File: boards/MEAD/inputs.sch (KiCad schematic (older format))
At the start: 13 parts, among them J3 LSHM-120-02.5-L-DV-A-N-K-TR, U10 RCLAMP0542T, U11 RCLAMP0542T, U12 RCLAMP0542T, U13 RCLAMP0542T

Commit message: Updated MEAD LA pod design with display and different protection diodes
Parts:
- removed U10, U11, U12, U13: RCLAMP0542T, symbol special-azonenberg:RCLAMP0542T
- added D10, D11, D12, D9: SP4010, symbol special-azonenberg:SP4010
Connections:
- net labels added: 5V0
- wire segments 66 -> 50
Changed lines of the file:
@@
 encoding utf-8
 Sheet 5 6
-Title ""
-Date "2020-05-26"
-Rev ""
-Comp ""
-Comment1 ""
+Title "Logic Analyzer Pod"
+Date "2020-05-28"
+Rev "0.1"
+Comp "Antikernel Labs"
+Comment1 "Andrew D. Zonenberg"
 Comment2 ""
 Comment3 ""
@@
 Text Label 1500 2500 2    50   ~ 0
 GND
-$Comp
-L special-azonenberg:RCLAMP0542T U10
-U 1 1 5ECE5387
-P 3650 1550
-F 0 "U10" H 3650 1500 60  0000 L CNN
-F 1 "RCLAMP0542T" H 3650 1400 60  0000 L CNN
-F 2 "" H 3650 1550 60  0000 C CNN
-F 3 "" H 3650 1550 60  0000 C CNN
-	1    3650 1550
-	1    0    0    -1
-$EndComp
-Text Label 3200 900  2    50   ~ 0
+Text Label 3350 1300 2    50   ~ 0
 CH0
-Wire Wire Line
-	3200 900  3350 900
-Wire Wire Line
-	3350 900  3350 1000
-Connection ~ 3350 900
-Text Label 3200 1100 2    50   ~ 0
+Text Label 3350 1400 2    50   ~ 0
 CH1
-Wire Wire Line
-	3200 1100 3350 1100
-Wire Wire Line
-	3350 1100 3350 1200
-Connection ~ 3350 1100
-Text Label 3200 1400 2    50   ~ 0
-GND
-Wire Wire Line
-	3200 1400 3350 1400
-Wire Wire Line
-	3350 1400 3350 1500
-Connection ~ 3350 1400
+Text Label 3350 1100 2    50   ~ 0
+GND
 Connection ~ 2000 2200
 Connection ~ 2000 1700
@@
 Text HLabel 2000 2800 2    50   BiDi ~ 0
 PROBE_I2C_SCL
-$Comp
-L special-azonenberg:RCLAMP0542T U11
-U 1 1 5ECE818C
-P 3650 2550
-F 0 "U11" H 3650 2500 60  0000 L CNN
-F 1 "RCLAMP0542T" H 3650 2400 60  0000 L CNN
-F 2 "" H 3650 2550 60  0000 C CNN
-F 3 "" H 3650 2550 60  0000 C CNN
-	1    3650 2550
-	1    0    0    -1
-$EndComp
-Text Label 3200 1900 2    50   ~ 0
+Text Label 3350 2250 2    50   ~ 0
 CH2
-Wire Wire Line
-	3200 1900 3350 1900
-Wire Wire Line
-	3350 1900 3350 2000
-Connection ~ 3350 1900
-Text Label 3200 2100 2    50   ~ 0
+Text Label 3350 2350 2    50   ~ 0
 CH3
-Wire Wire Line
-	3200 2100 3350 2100
-Wire Wire Line
-	3350 2100 3350 2200
-Connection ~ 3350 2100
-Text Label 3200 2400 2    50   ~ 0
-GND
-Wire Wire Line
-	3200 2400 3350 2400
-Wire Wire Line
-	3350 2400 3350 2500
-Connection ~ 3350 2400
-$Comp
-L special-azonenberg:RCLAMP0542T U12
-U 1 1 5ECE92F3
-P 5150 1550
-F 0 "U12" H 5150 1500 60  0000 L CNN
-F 1 "RCLAMP0542T" H 5150 1400 60  0000 L CNN
-F 2 "" H 5150 1550 60  0000 C CNN
-F 3 "" H 5150 1550 60  0000 C CNN
-	1    5150 1550
-	1    0    0    -1
-$EndComp
-Text Label 4700 900  2    50   ~ 0
+Text Label 3350 2050 2    50   ~ 0
+GND
+Text Label 4450 1300 2    50   ~ 0
 CH4
-Wire Wire Line
-	4700 900  4850 900
-Wire Wire Line
-	4850 900  4850 1000
-Connection ~ 4850 900
-Text Label 4700 1100 2    50   ~ 0
+Text Label 4450 1400 2    50   ~ 0
 CH5
-Wire Wire Line
-	4700 1100 4850 1100
-Wire Wire Line
-	4850 1100 4850 1200
-Connection ~ 4850 1100
-Text Label 4700 1400 2    50   ~ 0
-GND
-Wire Wire Line
-	4700 1400 4850 1400
-Wire Wire Line
-	4850 1400 4850 1500
-Connection ~ 4850 1400
-$Comp
-L special-azonenberg:RCLAMP0542T U13
-U 1 1 5ECE9309
-P 5150 2550
-F 0 "U13" H 5150 2500 60  0000 L CNN
-F 1 "RCLAMP0542T" H 5150 2400 60  0000 L CNN
-F 2 "" H 5150 2550 60  0000 C CNN
-F 3 "" H 5150 2550 60  0000 C CNN
-	1    5150 2550
-	1    0    0    -1
-$EndComp
-Text Label 4700 1900 2    50   ~ 0
+Text Label 4450 1100 2    50   ~ 0
+GND
+Text Label 4450 2250 2    50   ~ 0
 CH6
-Wire Wire Line
-	4700 1900 4850 1900
-Wire Wire Line
-	4850 1900 4850 2000
-Connection ~ 4850 1900
-Text Label 4700 2100 2    50   ~ 0
+Text Label 4450 2350 2    50   ~ 0
 CH7
-Wire Wire Line
-	4700 2100 4850 2100
-Wire Wire Line
-	4850 2100 4850 2200
-Connection ~ 4850 2100
-Text Label 4700 2400 2    50   ~ 0
-GND
-Wire Wire Line
-	4700 2400 4850 2400
-Wire Wire Line
-	4850 2400 4850 2500
-Connection ~ 4850 2400
 Text HLabel 1500 900  0    50   Input ~ 0
 GND
@@
 Wire Wire Line
 	2050 4850 2050 4750
+$Comp
+L special-azonenberg:SP4010 D9
+U 1 1 5EE05990
+P 3600 1450
+F 0 "D9" H 3600 1400 50  0000 L CNN
+F 1 "SP4010" H 3600 1300 50  0000 L CNN
+F 2 "" H 3600 1450 50  0001 C CNN
+F 3 "" H 3600 1450 50  0001 C CNN
+	1    3600 1450
+	1    0    0    -1
+$EndComp
+Text HLabel 3350 800  0    50   Input ~ 0
+5V0
+Wire Wire Line
+	3350 800  3350 900
+Connection ~ 3350 900
+Wire Wire Line
+	3350 900  3350 1000
+$Comp
+L special-azonenberg:SP4010 D10
+U 1 1 5EE0A3EE
+P 3600 2400
+F 0 "D10" H 3600 2350 50  0000 L CNN
+F 1 "SP4010" H 3600 2250 50  0000 L CNN
+F 2 "" H 3600 2400 50  0001 C CNN
+F 3 "" H 3600 2400 50  0001 C CNN
+	1    3600 2400
+	1    0    0    -1
+$EndComp
+Text Label 3350 1750 2    50   ~ 0
+5V0
+Wire Wire Line
+	3350 1750 3350 1850
+Connection ~ 3350 1850
+Wire Wire Line
+	3350 1850 3350 1950
+$Comp
+L special-azonenberg:SP4010 D11
+U 1 1 5EE0B83F
+P 4700 1450
+F 0 "D11" H 4700 1400 50  0000 L CNN
+F 1 "SP4010" H 4700 1300 50  0000 L CNN
+F 2 "" H 4700 1450 50  0001 C CNN
+F 3 "" H 4700 1450 50  0001 C CNN
+	1    4700 1450
+	1    0    0    -1
+$EndComp
+Text Label 4450 800  2    50   ~ 0
+5V0
+Wire Wire Line
+	4450 800  4450 900
+Connection ~ 4450 900
+Wire Wire Line
+	4450 900  4450 1000
+$Comp
+L special-azonenberg:SP4010 D12
+U 1 1 5EE0E0E3
+P 4700 2400
+F 0 "D12" H 4700 2350 50  0000 L CNN
+F 1 "SP4010" H 4700 2250 50  0000 L CNN
+F 2 "" H 4700 2400 50  0001 C CNN
+F 3 "" H 4700 2400 50  0001 C CNN
+	1    4700 2400
+	1    0    0    -1
+$EndComp
+Text Label 4450 2050 2    50   ~ 0
+GND
+Text Label 4450 1750 2    50   ~ 0
+5V0
+Wire Wire Line
+	4450 1750 4450 1850
+Connection ~ 4450 1850
+Wire Wire Line
+	4450 1850 4450 1950
 $EndSCHEMATC

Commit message: Updated LA pod schematic with additional ESD protection and noise filtering
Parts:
- D10, D11, D12, D9: footprint (none) -> azonenberg_pcb:SOT23_6
- J3: footprint (none) -> azonenberg_pcb:CONN_SAMTEC_LSHM-120-02.5-L-DV-A-N-K-TR
- R17, R19, R21, R23, R69, R7, R70, R71: footprint (none) -> azonenberg_pcb:EIA_0402_RES_NOSILK
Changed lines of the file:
@@
 F 0 "J3" H 1750 2917 50  0000 C CNN
 F 1 "LSHM-120-02.5-L-DV-A-N-K-TR" H 1750 2826 50  0000 C CNN
-F 2 "" H 1700 1800 50  0001 C CNN
+F 2 "azonenberg_pcb:CONN_SAMTEC_LSHM-120-02.5-L-DV-A-N-K-TR" H 1700 1800 50  0001 C CNN
 F 3 "~" H 1700 1800 50  0001 C CNN
 	1    1700 1800
@@
 F 0 "R7" V 1700 4000 50  0000 C CNN
 F 1 "49.9" V 1750 4250 50  0000 C CNN
-F 2 "" V 1680 4250 50  0001 C CNN
+F 2 "azonenberg_pcb:EIA_0402_RES_NOSILK" V 1680 4250 50  0001 C CNN
 F 3 "" H 1750 4250 50  0001 C CNN
 	1    1750 4250
@@
 F 0 "R17" V 1700 4100 50  0000 C CNN
 F 1 "49.9" V 1750 4350 50  0000 C CNN
-F 2 "" V 1680 4350 50  0001 C CNN
+F 2 "azonenberg_pcb:EIA_0402_RES_NOSILK" V 1680 4350 50  0001 C CNN
 F 3 "" H 1750 4350 50  0001 C CNN
 	1    1750 4350
@@
 F 0 "R19" V 1700 4200 50  0000 C CNN
 F 1 "49.9" V 1750 4450 50  0000 C CNN
-F 2 "" V 1680 4450 50  0001 C CNN
+F 2 "azonenberg_pcb:EIA_0402_RES_NOSILK" V 1680 4450 50  0001 C CNN
 F 3 "" H 1750 4450 50  0001 C CNN
 	1    1750 4450
@@
 F 0 "R21" V 1700 4300 50  0000 C CNN
 F 1 "49.9" V 1750 4550 50  0000 C CNN
-F 2 "" V 1680 4550 50  0001 C CNN
+F 2 "azonenberg_pcb:EIA_0402_RES_NOSILK" V 1680 4550 50  0001 C CNN
 F 3 "" H 1750 4550 50  0001 C CNN
 	1    1750 4550
@@
 F 0 "R23" V 1700 4400 50  0000 C CNN
 F 1 "49.9" V 1750 4650 50  0000 C CNN
-F 2 "" V 1680 4650 50  0001 C CNN
+F 2 "azonenberg_pcb:EIA_0402_RES_NOSILK" V 1680 4650 50  0001 C CNN
 F 3 "" H 1750 4650 50  0001 C CNN
 	1    1750 4650
@@
 F 0 "R69" V 1700 4500 50  0000 C CNN
 F 1 "49.9" V 1750 4750 50  0000 C CNN
-F 2 "" V 1680 4750 50  0001 C CNN
+F 2 "azonenberg_pcb:EIA_0402_RES_NOSILK" V 1680 4750 50  0001 C CNN
 F 3 "" H 1750 4750 50  0001 C CNN
 	1    1750 4750
@@
 F 0 "R70" V 1700 4600 50  0000 C CNN
 F 1 "49.9" V 1750 4850 50  0000 C CNN
-F 2 "" V 1680 4850 50  0001 C CNN
+F 2 "azonenberg_pcb:EIA_0402_RES_NOSILK" V 1680 4850 50  0001 C CNN
 F 3 "" H 1750 4850 50  0001 C CNN
 	1    1750 4850
@@
 F 0 "R71" V 1700 4700 50  0000 C CNN
 F 1 "49.9" V 1750 4950 50  0000 C CNN
-F 2 "" V 1680 4950 50  0001 C CNN
+F 2 "azonenberg_pcb:EIA_0402_RES_NOSILK" V 1680 4950 50  0001 C CNN
 F 3 "" H 1750 4950 50  0001 C CNN
 	1    1750 4950
@@
 F 0 "D9" H 3600 1400 50  0000 L CNN
 F 1 "SP4010" H 3600 1300 50  0000 L CNN
-F 2 "" H 3600 1450 50  0001 C CNN
+F 2 "azonenberg_pcb:SOT23_6" H 3600 1450 50  0001 C CNN
 F 3 "" H 3600 1450 50  0001 C CNN
 	1    3600 1450
@@
 F 0 "D10" H 3600 2350 50  0000 L CNN
 F 1 "SP4010" H 3600 2250 50  0000 L CNN
-F 2 "" H 3600 2400 50  0001 C CNN
+F 2 "azonenberg_pcb:SOT23_6" H 3600 2400 50  0001 C CNN
 F 3 "" H 3600 2400 50  0001 C CNN
 	1    3600 2400
@@
 F 0 "D11" H 4700 1400 50  0000 L CNN
 F 1 "SP4010" H 4700 1300 50  0000 L CNN
-F 2 "" H 4700 1450 50  0001 C CNN
+F 2 "azonenberg_pcb:SOT23_6" H 4700 1450 50  0001 C CNN
 F 3 "" H 4700 1450 50  0001 C CNN
 	1    4700 1450
@@
 F 0 "D12" H 4700 2350 50  0000 L CNN
 F 1 "SP4010" H 4700 2250 50  0000 L CNN
-F 2 "" H 4700 2400 50  0001 C CNN
+F 2 "azonenberg_pcb:SOT23_6" H 4700 2400 50  0001 C CNN
 F 3 "" H 4700 2400 50  0001 C CNN
 	1    4700 2400

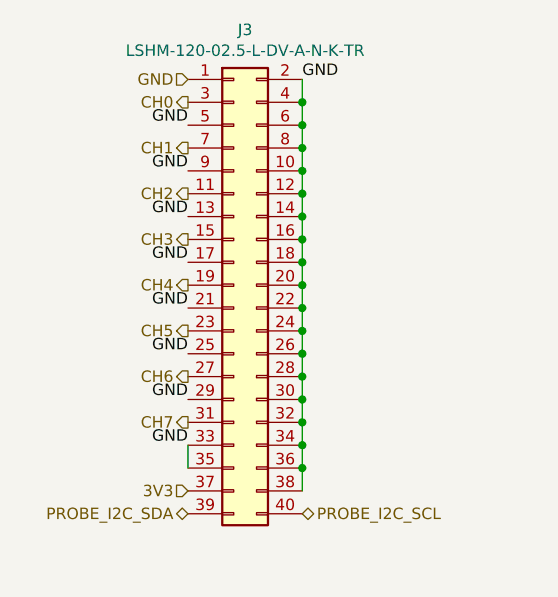
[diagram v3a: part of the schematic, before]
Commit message: Updating file: la-pod.kicad_pcb with current fully routed design
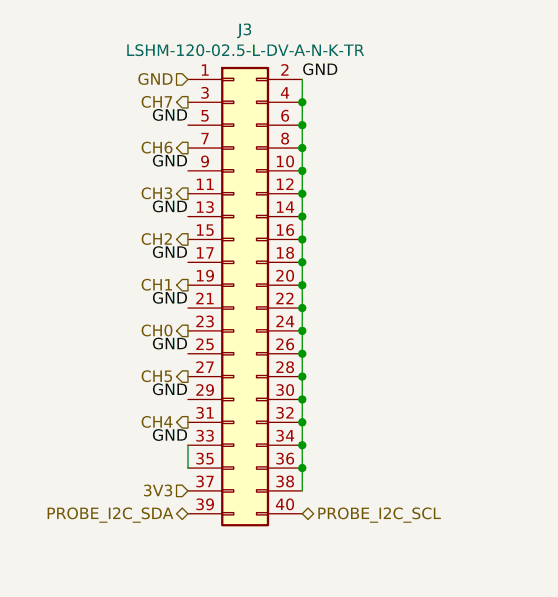
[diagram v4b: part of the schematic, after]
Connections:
- net CH0: now also J3.23 (Pin_23); no longer J3.3 (Pin_3)
- net CH1: now also J3.19 (Pin_19); no longer J3.7 (Pin_7)
- net CH2: now also J3.15 (Pin_15); no longer J3.11 (Pin_11)
- net CH3: now also J3.11 (Pin_11); no longer J3.15 (Pin_15)
- net CH4: now also J3.31 (Pin_31); no longer J3.19 (Pin_19)
- net CH5: now also J3.27 (Pin_27); no longer J3.23 (Pin_23)
- net CH6: now also J3.7 (Pin_7); no longer J3.27 (Pin_27)
- net CH7: now also J3.3 (Pin_3); no longer J3.31 (Pin_31)
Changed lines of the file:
@@
 Sheet 5 6
 Title "Logic Analyzer Pod"
-Date "2020-05-29"
+Date "2020-05-30"
 Rev "0.1"
 Comp "Antikernel Labs"
@@
 Comment4 ""
 $EndDescr
+Text HLabel 1500 2000 0    50   Output ~ 0
+CH0
+Text HLabel 1500 1800 0    50   Output ~ 0
+CH1
+Text HLabel 1500 1600 0    50   Output ~ 0
+CH2
+Text HLabel 1500 1400 0    50   Output ~ 0
+CH3
+Text HLabel 1500 2400 0    50   Output ~ 0
+CH4
+Text HLabel 1500 2200 0    50   Output ~ 0
+CH5
+Text HLabel 1500 1200 0    50   Output ~ 0
+CH6
 Text HLabel 1500 1000 0    50   Output ~ 0
-CH0
-Text HLabel 1500 1200 0    50   Output ~ 0
-CH1
-Text HLabel 1500 1400 0    50   Output ~ 0
-CH2
-Text HLabel 1500 1600 0    50   Output ~ 0
-CH3
-Text HLabel 1500 1800 0    50   Output ~ 0
-CH4
-Text HLabel 1500 2000 0    50   Output ~ 0
-CH5
-Text HLabel 1500 2200 0    50   Output ~ 0
-CH6
-Text HLabel 1500 2400 0    50   Output ~ 0
 CH7
 Text Label 2000 900  0    50   ~ 0
